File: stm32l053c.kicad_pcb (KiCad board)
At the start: 2 copper layers, 20.8 x 43.7 mm, 21 parts, among them P1 SWD, P2 CONN_01X17, P3 CONN_01X17, P4 Ext Xtal, U1 STM32L053C8_LQFP48

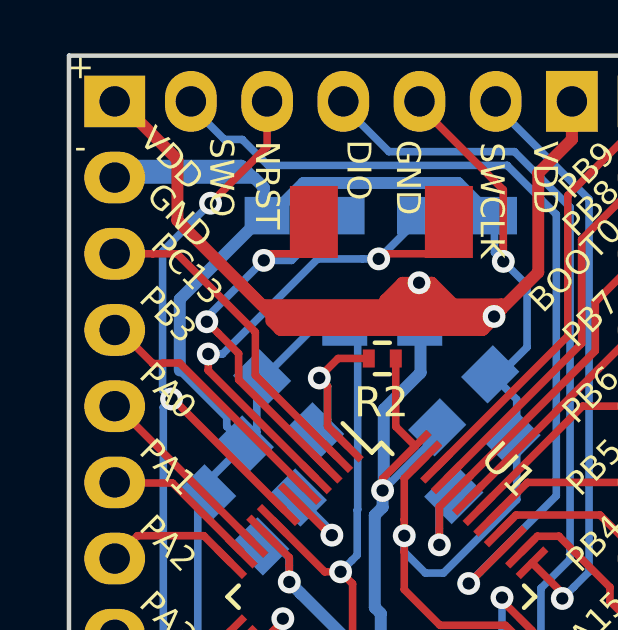
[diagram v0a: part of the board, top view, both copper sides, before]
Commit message: Fixed the label for MCO
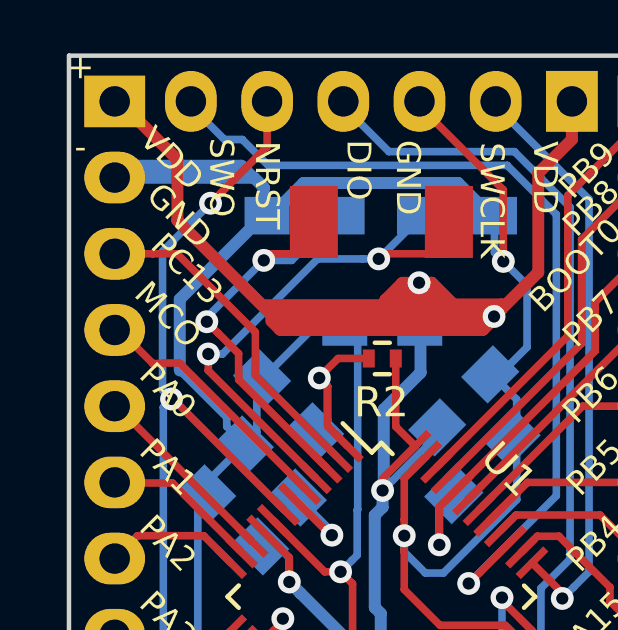
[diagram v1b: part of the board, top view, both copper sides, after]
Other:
- board text added: "MCO"
- board text removed: "PB3"
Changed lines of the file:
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@@
   (page A4)
   (layers
-    (0 F.Cu signal hide)
+    (0 F.Cu signal)
     (31 B.Cu signal hide)
     (32 B.Adhes user)
@@
     (effects (font (size 0.8 0.8) (thickness 0.15)))
   )
-  (gr_text PB3 (at 184.658 88.392 315) (layer F.SilkS)
-    (effects (font (size 0.8 0.8) (thickness 0.15)))
-  )
+  (gr_text MCO (at 184.658 88.392 315) (layer F.SilkS)
+    (effects (font (size 0.8 0.8) (thickness 0.15)))
+  )
